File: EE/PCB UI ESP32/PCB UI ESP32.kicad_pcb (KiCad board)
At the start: 2 copper layers, 94.8 x 94.8 mm, 58 parts, among them J1 T1M-05-F-SV-L, J2 T1M-02-F-SV-L, J3 KH-TYPE-C-16P, Q1 SS8050, Q2 SS8050, SW1 EN, U1 CH340C, U11 693063020911, U12 MCP1826ST-3302E_DB, U2 ESP32-WROOM-32E, U5 PEC16-4215F-S0024, U7 PESD3V3L1BA, U8 DW-20-07-T-S-200, U9 PESD3V3L1BA

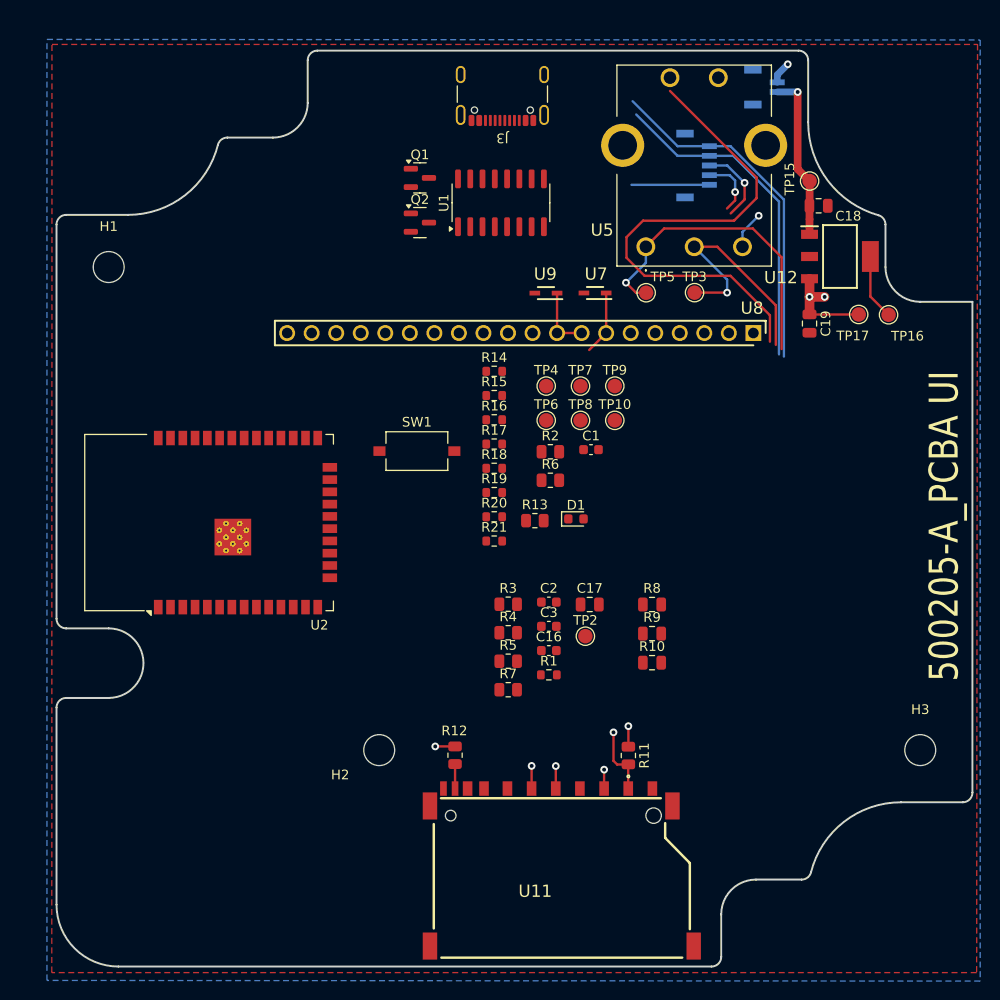
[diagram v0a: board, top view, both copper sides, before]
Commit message: Finished first draft of ESP32-UI board
And moved around footprints, 3D models, etc. to match.
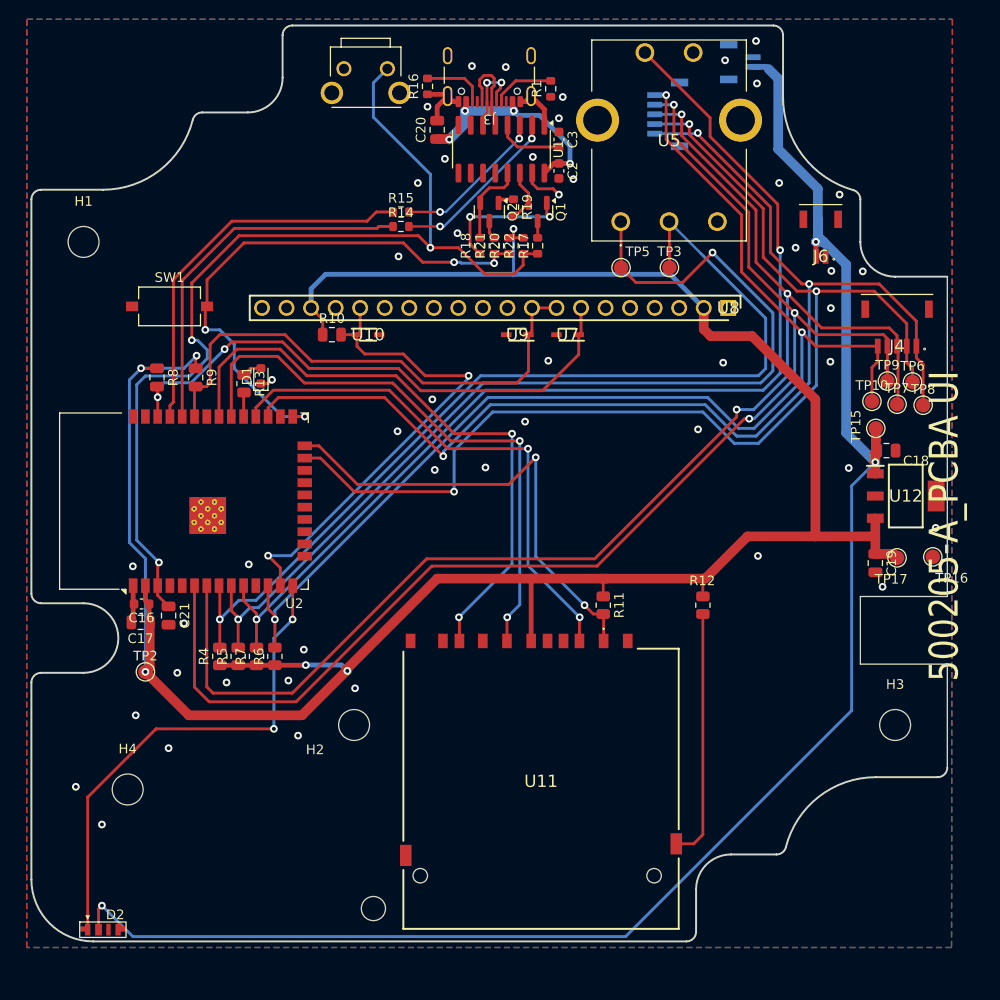
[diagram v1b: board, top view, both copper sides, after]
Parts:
- removed C1: 100 nF, Capacitor_SMD:C_0603_1608Metric
- removed R2: 10K, Resistor_SMD:R_0805_2012Metric
- removed R3: 1K, Resistor_SMD:R_0805_2012Metric
- removed TP4: TestPoint, TestPoint:TestPoint_Pad_D1.5mm
- added C20: 10 uF, Capacitor_SMD:C_0805_2012Metric, F.Cu at (92.0, 60.8)
- added C21: 10 uF, Capacitor_SMD:C_0805_2012Metric, F.Cu at (64.2, 111.1)
- added D2: SK6812-SIDE-A, DaisyBio_Mira:SK6812-SIDE-A, F.Cu at (55.8, 143.6)
- added H4: Plated 2.55mm Hole, MountingHole:MountingHole_3.2mm_M3, F.Cu at (60.0, 129.1)
- added J4: T1M-05-F-SH-L, DaisyBio_Mira:T1M-05-X-SH-L, F.Cu at (139.6, 83.2)
- added J6: T1M-02-F-SH-L, DaisyBio_Mira:T1M-02-X-SH-L, F.Cu at (131.7, 73.9)
- added R22: 10k, Resistor_SMD:R_0603_1608Metric, F.Cu at (100.9, 72.8)
- added S1: B3F-3100, DaisyBio_Mira:B3F3100, F.Cu at (84.6, 52.2)
- added U10: PESD3V3L1BA, DaisyBio_Mira:SOD2512X110N, F.Cu at (84.8, 82.0)
- J1: footprint T1M-05-F-SV-L:T1M05FSVL -> DaisyBio_Mira:T1M-05-X-SV-L-Y
- J2: footprint T1M-02-F-SV-L:T1M02FSVL -> DaisyBio_Mira:T1M02FSVL
- U11: value 693063020911 -> 10067847001RLF; footprint 6930630220911:693063020911 -> DaisyBio_Mira:10067847001RLF
- U12: footprint MCP1826ST-3302E_DB:SOT230P700X180-4N -> DaisyBio_Mira:SOT230P700X180-4N
- U5: footprint PEC16-4215F-S0024:PEC164120FS0012 -> DaisyBio_Mira:PEC164120FS0012
- U7, U9: footprint PESD3V3L1BA:SOD2512X110N -> DaisyBio_Mira:SOD2512X110N
- U8: footprint DW-20-07-T-S-200:HDRV20W64P0X254_1X20_5080X254X1067P -> DaisyBio_Mira:HDRV20W64P0X254_1X20_5080X254X1067P
- moved R1 60.7 mm to (103.8, 56.5), turned to 90 degrees
- moved R8 56.4 mm to (63.0, 86.4), turned to -90 degrees
- moved R9 54.2 mm to (67.0, 86.4), turned to -90 degrees
- moved C3 50.4 mm to (104.6, 61.8), turned to -90 degrees
- moved R10 47.4 mm to (81.1, 82.0)
- moved C17 46.5 mm to (61.3, 111.8), turned to 180 degrees
- moved TP2 45.7 mm to (61.8, 116.9)
- moved C2 44.6 mm to (104.6, 65.0), turned to -90 degrees
- moved C16 42.4 mm to (61.4, 109.9), turned to 180 degrees
- moved TP6 38.1 mm to (141.2, 86.9)
- moved D1 35.8 mm to (73.8, 86.3), turned to 90 degrees
- moved TP8 35.5 mm to (142.3, 89.3)
- moved R16 35.2 mm to (91.0, 56.3), turned to 90 degrees
- moved R6 33.8 mm to (75.2, 115.3), turned to 90 degrees
- moved R13 33.3 mm to (72.0, 87.1), turned to -90 degrees
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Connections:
- net Net-(U1-UD+) renamed /Microcontroller/D+
- net Net-(U1-UD-) renamed /Microcontroller/D-
- U2 pad 10: THRM -> SW ENC
- U2 pad 12: SW ENC -> THRM
- U2 pad 14: unconnected-(U2-IO12-Pad14) -> /Microcontroller/LED_DEBUG
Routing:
- net +3V3: track 16.9 -> 252.2 mm, vias 5 -> 6
- net +5V: track 17.4 -> 174.1 mm, vias 1 -> 3
- net HTR_PID: track 6.13 -> 137.7 mm, vias 1 -> 3
- net BLWR_PID: track 8.15 -> 139.3 mm, vias 1 -> 3
- net THRM: track 8.06 -> 125.7 mm, vias 0 -> 3
- net /Microcontroller/EN: track 0.00 -> 104.3 mm, vias 0 -> 3
- net MTR_PID1: track 36.1 -> 123.1 mm, vias 0 -> 3
- net MTR_PID2: track 34.3 -> 118.4 mm, vias 0 -> 3
- net CH/B ENC: track 24.6 -> 97.6 mm
- net CH/A ENC: track 32.7 -> 103.7 mm, vias 1 -> 2
- net SD_MISO: track 0.00 -> 63.6 mm, vias 0 -> 2
- net SW ENC: track 52.1 -> 110.7 mm, vias 0 -> 2
- net SD_SCLK: track 2.35 -> 60.5 mm, vias 1 -> 2
- net /Microcontroller/BOOT: track 0.00 -> 56.4 mm, vias 0 -> 4
- net SD_MOSI: track 1.96 -> 54.5 mm, vias 1 -> 2
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- added copper zone on B.Cu, net GND
- removed copper zone on B.Cu, net +3V3
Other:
- outline, holes or cut-outs redrawn
- board text added: "Project Mira UI PCB R2"

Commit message: Finished V1 of ESP-UI
This is the version of ESP-UI that was ordered July 20 2025.
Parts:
- removed U11: 10067847001RLF, DaisyBio_Mira:10067847001RLF
- added J5: 10067847-001RLF, DaisyBio_Mira:10067847001RLF, F.Cu at (102.8, 129.0)
- moved TP6 43.5 mm to (125.0, 127.2)
- moved TP8 39.2 mm to (125.0, 124.5)
- moved TP7 35.7 mm to (125.0, 121.8)
- moved TP9 32.4 mm to (125.0, 116.2)
- moved TP10 32.4 mm to (125.0, 119.0)
- moved TP16 31.0 mm to (125.0, 130.0)
- moved TP15 25.1 mm to (125.0, 113.5)
- moved TP17 15.7 mm to (125.0, 110.8)
- moved R12 14.4 mm to (105.1, 110.0)
- moved TP2 3.44 mm to (64.0, 114.2)
- moved R9 3.00 mm to (70.0, 86.5)
- moved J4 2.60 mm to (137.0, 83.2)
- moved C16 2.25 mm to (63.6, 109.9)
- moved C17 2.25 mm to (63.5, 111.8)
- moved C21 2.25 mm to (66.5, 111.1)
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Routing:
- net MTR_PID2: track 118.4 -> 171.6 mm, vias 3 -> 5
- net MTR_PID1: track 123.1 -> 172.1 mm, vias 3 -> 5
- net BLWR_PID: track 139.3 -> 183.8 mm, vias 3 -> 5
- net THRM: track 125.7 -> 166.5 mm, vias 3 -> 5
- net HTR_PID: track 137.7 -> 178.3 mm, vias 3 -> 5
- net SD_CARD_DET: track 26.0 -> 2.80 mm
- net +3V3: track 252.2 -> 271.0 mm
- net +5V: track 174.1 -> 166.3 mm, vias 3 -> 4
- net /Microcontroller/EN: track 104.3 -> 97.8 mm
- net /Microcontroller/LED_DEBUG: track 51.5 -> 46.6 mm
- net SCL_DISP: track 58.1 -> 55.0 mm
- net SDA_DISP: track 53.8 -> 51.3 mm
- net /RES_DISP: track 50.8 -> 48.3 mm
- net SD_SCLK: track 60.5 -> 58.3 mm
- net SD_CS: track 49.2 -> 47.0 mm
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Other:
- outline, holes or cut-outs redrawn
- board text added: "+3V3"
- board text added: "+3V3 +5V HEATER PID THERM BLOWER PID MOTOR PID 1 MOTOR PID 2 GND"
- board text added: "500273-A_PCBA UI ESP32"
- board text added: "BOOT"
- board text added: "ENC CH A CH B"
- board text added: "GND"
- board text added: "RESET"
- board text removed: "500205-A_PCBA UI"
